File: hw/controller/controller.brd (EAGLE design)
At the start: 46 x 53 mm, 105 parts, among them J1 XT30XT30PW_MALE, J2 XT30XT30PW_MALE, M1 MOUNT, M2 MOUNT, M3 MOUNT, M4 MOUNT, Q1 TPH1R204PLSOP_ADVANCE_8, Q2 TPH1R204PLSOP_ADVANCE_8, Q3 TPH1R204PLSOP_ADVANCE_8, Q4 TPH1R204PLSOP_ADVANCE_8, Q5 TPH1R204PLSOP_ADVANCE_8, Q6 TPH1R204PLSOP_ADVANCE_8, U1 STM32G474CEU6, U2 TCAN334GSOT23, U3 AS5147, U4 DRV8323RS

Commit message: Initial work on r4.5
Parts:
- A, B, C: value PAD -> PAD16AWG_PAD; device controller:18AWG_PAD -> controller:16AWG_PAD
- R6: value 10k 1% -> 4.7k 1%
- moved A 0.98 mm to (-14.5, -28.2)
- moved C 0.98 mm to (14.5, -28.2)
- moved B 0.40 mm to (0.00, -28.2)
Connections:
- net GND: now also U1.38; no longer U1.29
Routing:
- net GND: track 93.0 -> 95.1 mm, vias 35 -> 34
- net +3V3: track 117.0 -> 118.0 mm
- net V-: vias 48 -> 50
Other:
- board text added: "moteus r4.5"
- board text removed: "moteus r4.4"

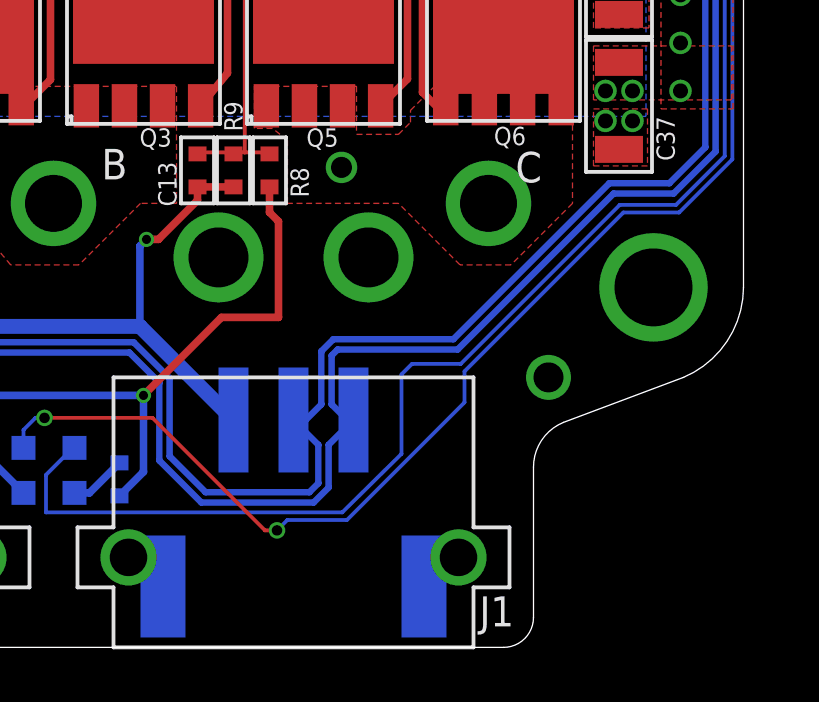
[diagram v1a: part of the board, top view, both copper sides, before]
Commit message: Add test through holes for the CAN bus on a 2mm spacing
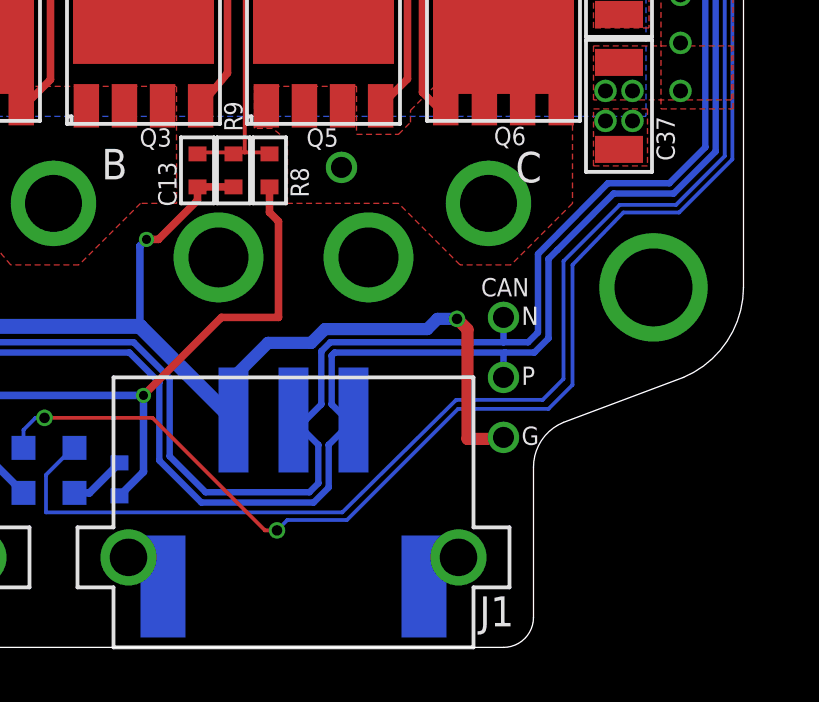
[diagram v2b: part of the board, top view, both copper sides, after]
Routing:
- net GND: track 95.1 -> 110.1 mm, vias 34 -> 36
- net CAN_P: track 58.7 -> 61.1 mm, vias 1 -> 2
- net CAN_N: track 59.3 -> 61.7 mm, vias 1 -> 2
- net LED1: track 84.7 -> 86.5 mm
- net LED2: track 77.3 -> 78.0 mm
- net V-: vias 50 -> 49
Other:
- board text added: "CAN"
- board text added: "N"
- board text added: "P"
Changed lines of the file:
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@@
 <vertex x="9.48" y="-4.93"/>
 </polygon>
+<text x="15.6" y="-32.25" size="0.6096" layer="21" font="vector">N</text>
+<text x="15.6" y="-34.25" size="0.6096" layer="21" font="vector">P</text>
+<text x="15.6" y="-36.25" size="0.6096" layer="21" font="vector">G</text>
+<text x="14.25" y="-31.3" size="0.6096" layer="21" font="vector">CAN</text>
 </plain>
 <attributes>
@@
 </polygon>
 <via x="-16.5" y="-34" extent="1-16" drill="1"/>
-<via x="16.5" y="-34" extent="1-16" drill="1"/>
 </signal>
 <signal name="CUR3">
@@
 <wire x1="7.45" y1="-39.1" x2="7.796" y2="-38.754" width="0.127" layer="16"/>
 <wire x1="7.796" y1="-38.754" x2="9.7802125" y2="-38.754" width="0.127" layer="16"/>
-<wire x1="13.7" y1="-34.8342125" x2="13.7" y2="-33.8" width="0.127" layer="16"/>
-<wire x1="9.7802125" y1="-38.754" x2="13.7" y2="-34.8342125" width="0.127" layer="16"/>
+<wire x1="9.7802125" y1="-38.754" x2="13.4842125" y2="-35.05" width="0.127" layer="16"/>
 <wire x1="22.629" y1="-11.521" x2="22.65" y2="-11.5" width="0.127" layer="16"/>
 <wire x1="20.8552125" y1="-28.504" x2="22.629" y2="-26.7302125" width="0.127" layer="16"/>
 <wire x1="22.629" y1="-26.7302125" x2="22.629" y2="-11.521" width="0.127" layer="16"/>
-<wire x1="13.7" y1="-33.8" x2="18.996" y2="-28.504" width="0.127" layer="16"/>
+<wire x1="13.4842125" y1="-35.05" x2="16.5" y2="-35.05" width="0.127" layer="16"/>
+<wire x1="16.5" y1="-35.05" x2="17.3" y2="-34.25" width="0.127" layer="16"/>
+<wire x1="17.3" y1="-34.25" x2="17.3" y2="-30.25" width="0.127" layer="16"/>
+<wire x1="17.3" y1="-30.25" x2="18.996" y2="-28.504" width="0.127" layer="16"/>
 <wire x1="18.996" y1="-28.504" x2="20.8552125" y2="-28.504" width="0.127" layer="16"/>
 <wire x1="22.65" y1="-11.5" x2="22.65" y2="-0.95" width="0.127" layer="16"/>
@@
 <wire x1="-0.25" y1="-38.5" x2="-0.25" y2="-37.25" width="0.127" layer="16"/>
 <wire x1="9.625" y1="-38.5" x2="-0.25" y2="-38.5" width="0.127" layer="16"/>
-<wire x1="18.875" y1="-28.25" x2="13.575" y2="-33.55" width="0.127" layer="16"/>
-<wire x1="13.575" y1="-33.55" x2="11.95" y2="-33.55" width="0.127" layer="16"/>
-<wire x1="11.95" y1="-33.55" x2="11.6" y2="-33.9" width="0.127" layer="16"/>
-<wire x1="11.6" y1="-33.9" x2="11.6" y2="-36.55" width="0.127" layer="16"/>
-<wire x1="11.6" y1="-36.55" x2="9.625" y2="-38.5" width="0.127" layer="16"/>
+<wire x1="18.875" y1="-28.25" x2="17" y2="-30.125" width="0.127" layer="16"/>
+<wire x1="17" y1="-30.125" x2="17" y2="-34.05" width="0.127" layer="16"/>
+<wire x1="17" y1="-34.05" x2="16.303728125" y2="-34.749915625" width="0.127" layer="16"/>
+<wire x1="16.303728125" y1="-34.749915625" x2="13.42226875" y2="-34.75000625" width="0.127" layer="16"/>
+<wire x1="13.42226875" y1="-34.75000625" x2="13.4" y2="-34.772784375" width="0.127" layer="16"/>
+<wire x1="13.4" y1="-34.772784375" x2="9.625" y2="-38.5" width="0.127" layer="16"/>
 <wire x1="20.75" y1="-28.25" x2="18.875" y2="-28.25" width="0.127" layer="16"/>
 <wire x1="22.375" y1="-26.625" x2="20.75" y2="-28.25" width="0.127" layer="16"/>
@@
 <wire x1="10.55" y1="6.35" x2="10.55" y2="5.05" width="0.1524" layer="1"/>
 <wire x1="10.55" y1="5.05" x2="9.9" y2="4.4" width="0.1524" layer="1"/>
+<via x="15" y="-36" extent="1-16" drill="0.7"/>
+<wire x1="6" y1="-35.42" x2="6" y2="-34" width="0.4064" layer="16"/>
+<wire x1="12.4596" y1="-32.3904" x2="12.8" y2="-32.05" width="0.4064" layer="16"/>
+<wire x1="8.5878875" y1="-32.85" x2="9.0474875" y2="-32.3904" width="0.4064" layer="16"/>
+<wire x1="9.0474875" y1="-32.3904" x2="12.4596" y2="-32.3904" width="0.4064" layer="16"/>
+<wire x1="12.8" y1="-32.05" x2="13.45" y2="-32.05" width="0.4064" layer="16"/>
+<via x="13.45" y="-32.05" extent="1-16" drill="0.35"/>
+<wire x1="13.45" y1="-32.05" x2="13.8" y2="-32.4" width="0.4064" layer="1"/>
+<wire x1="13.8" y1="-32.4" x2="13.8" y2="-36.05" width="0.4064" layer="1"/>
+<wire x1="13.8" y1="-36.05" x2="14.95" y2="-36.05" width="0.4064" layer="1"/>
+<wire x1="14.95" y1="-36.05" x2="15" y2="-36" width="0.4064" layer="1"/>
+<wire x1="6" y1="-34" x2="7.15" y2="-32.85" width="0.4064" layer="16"/>
+<wire x1="7.15" y1="-32.85" x2="8.5878875" y2="-32.85" width="0.4064" layer="16"/>
 </signal>
 <signal name="VTEMP_FET">
@@
 <wire x1="20.675" y1="-11.45" x2="20.675" y2="-13.174453125" width="0.2159" layer="1"/>
 <wire x1="21.462515625" y1="-13.96196875" x2="20.675" y2="-13.174453125" width="0.2159" layer="1"/>
-<wire x1="9.47101875" y1="-33.07145" x2="9.27145" y2="-33.27101875" width="0.2159" layer="16"/>
+<wire x1="9.37101875" y1="-33.17145" x2="9.27145" y2="-33.27101875" width="0.2159" layer="16"/>
 <wire x1="9.27145" y1="-33.27101875" x2="9.27145" y2="-34.9" width="0.2159" layer="16"/>
 <wire x1="9.27145" y1="-34.9" x2="9.79145" y2="-35.42" width="0.2159" layer="16"/>
@@
 <wire x1="22.07145" y1="-26.47101875" x2="20.67101875" y2="-27.87145" width="0.2159" layer="16"/>
 <wire x1="20.67101875" y1="-27.87145" x2="18.67101875" y2="-27.87145" width="0.2159" layer="16"/>
-<wire x1="18.67101875" y1="-27.87145" x2="13.47101875" y2="-33.07145" width="0.2159" layer="16"/>
-<wire x1="13.47101875" y1="-33.07145" x2="9.47101875" y2="-33.07145" width="0.2159" layer="16"/>
+<wire x1="18.67101875" y1="-27.87145" x2="16.8" y2="-29.75" width="0.2159" layer="16"/>
+<wire x1="16.8" y1="-29.75" x2="16.5" y2="-30.05" width="0.2159" layer="16"/>
+<wire x1="16.5" y1="-30.05" x2="16.5" y2="-32.7" width="0.2159" layer="16"/>
+<wire x1="16.5" y1="-32.7" x2="16.02855" y2="-33.17145" width="0.2159" layer="16"/>
+<wire x1="16.02855" y1="-33.17145" x2="15.05" y2="-33.17145" width="0.2159" layer="16"/>
+<wire x1="15.05" y1="-33.17145" x2="9.37101875" y2="-33.17145" width="0.2159" layer="16"/>
 <wire x1="22.07145" y1="-14.570903125" x2="21.462515625" y2="-13.96196875" width="0.2159" layer="16"/>
+<via x="15" y="-34" extent="1-16" drill="0.7"/>
+<wire x1="15" y1="-34" x2="15" y2="-33.22145" width="0.2159" layer="16"/>
+<wire x1="15" y1="-33.22145" x2="15.05" y2="-33.17145" width="0.2159" layer="16"/>
 </signal>
 <signal name="CAN_N" class="1">
@@
 <wire x1="20.8341" y1="-14.12656875" x2="20.05143125" y2="-13.3439" width="0.2159" layer="1"/>
 <via x="20.8341" y="-14.189428125" extent="1-16" drill="0.1016"/>
-<wire x1="9.32898125" y1="-32.72855" x2="8.92855" y2="-33.12898125" width="0.2159" layer="16"/>
+<wire x1="9.22898125" y1="-32.82855" x2="8.92855" y2="-33.12898125" width="0.2159" layer="16"/>
 <wire x1="8.92855" y1="-33.12898125" x2="8.92855" y2="-34.9" width="0.2159" layer="16"/>
 <wire x1="8.92855" y1="-34.9" x2="8.40855" y2="-35.42" width="0.2159" layer="16"/>
@@
 <wire x1="21.72855" y1="-15.083878125" x2="21.72855" y2="-26.32898125" width="0.2159" layer="16"/>
 <wire x1="21.72855" y1="-26.32898125" x2="20.52898125" y2="-27.52855" width="0.2159" layer="16"/>
-<wire x1="20.52898125" y1="-27.52855" x2="18.52898125" y2="-27.52855" width="0.2159" layer="16"/>
-<wire x1="18.52898125" y1="-27.52855" x2="13.32898125" y2="-32.72855" width="0.2159" layer="16"/>
-<wire x1="13.32898125" y1="-32.72855" x2="9.32898125" y2="-32.72855" width="0.2159" layer="16"/>
+<wire x1="20.52898125" y1="-27.52855" x2="18.47965" y2="-27.52855" width="0.2159" layer="16"/>
+<wire x1="18.47965" y1="-27.52855" x2="16.15" y2="-29.888825" width="0.2159" layer="16"/>
+<wire x1="16.15" y1="-29.888825" x2="16.15" y2="-32.5" width="0.2159" layer="16"/>
+<wire x1="16.15" y1="-32.5" x2="15.82145" y2="-32.82855" width="0.2159" layer="16"/>
+<wire x1="15.82145" y1="-32.82855" x2="15" y2="-32.82855" width="0.2159" layer="16"/>
+<wire x1="15" y1="-32.82855" x2="9.22898125" y2="-32.82855" width="0.2159" layer="16"/>
 <wire x1="21.72855" y1="-15.083878125" x2="20.8341" y2="-14.189428125" width="0.2159" layer="16"/>
+<via x="15" y="-32" extent="1-16" drill="0.7"/>
+<wire x1="15" y1="-32" x2="15" y2="-32.82855" width="0.2159" layer="16"/>
 </signal>
 <signal name="DAC">
